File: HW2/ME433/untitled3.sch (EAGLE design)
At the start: 22 parts

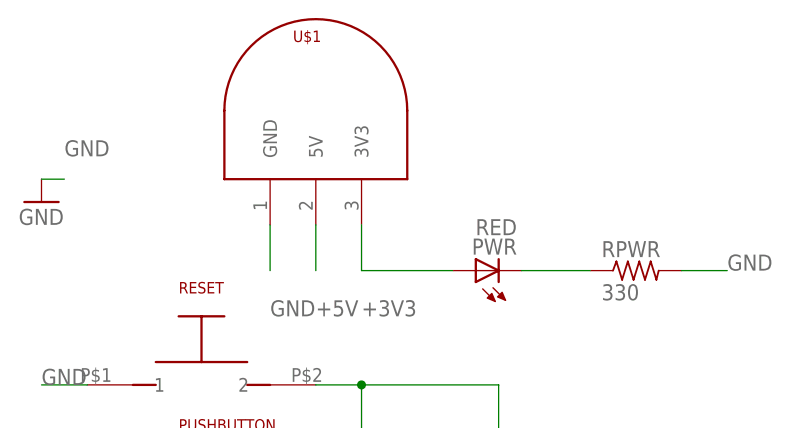
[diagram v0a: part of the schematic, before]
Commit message: Ready to be checked before order
updated voltage regulator package to TO-92 EBC and tweaked power traces
to avoid drill holes
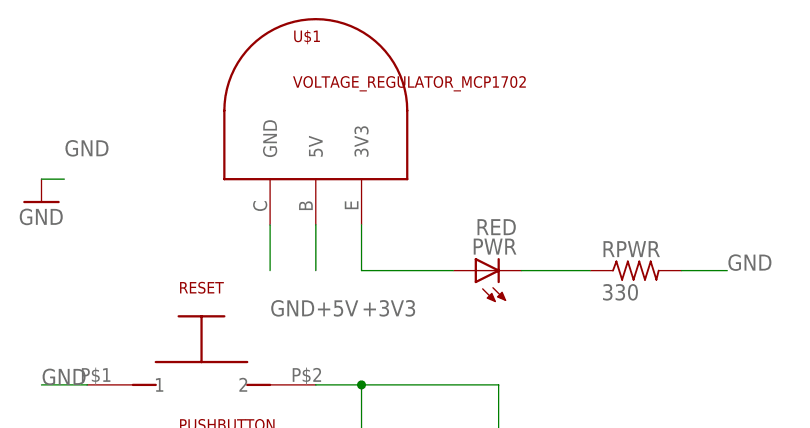
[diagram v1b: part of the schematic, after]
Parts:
- U$1: value VOLTAGE_REGULATOR_MCP1702TO92 -> VOLTAGE_REGULATOR_MCP1702; device components:VOLTAGE_REGULATOR_MCP1702TO92 -> components:VOLTAGE_REGULATOR_MCP1702
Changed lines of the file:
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@@
 </classes>
 <parts>
-<part name="U$1" library="components" deviceset="VOLTAGE_REGULATOR_MCP1702" device="TO92" value=""/>
+<part name="U$1" library="components" deviceset="VOLTAGE_REGULATOR_MCP1702" device="" value="VOLTAGE_REGULATOR_MCP1702"/>
 <part name="USER" library="components" deviceset="TLLG4400" device="" value="USER"/>
 <part name="BUTTON" library="components" deviceset="R-US_" device="0207/10" value="10k"/>
